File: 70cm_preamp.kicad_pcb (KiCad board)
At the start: 2 copper layers, 33 x 13.2 mm, 7 parts, among them J1 RF_IN, J2 RF_OUT, U1 SF2446E, U2 PGA-103+

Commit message: Stabilitáshoz RLC
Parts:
- added C1: 330p, 70cm_preamp:C_0603_1608Metric_Pad1.05x0.95mm_HandSolder, F.Cu at (63.1, 40.2)
- added L1: 620n, 70cm_preamp:L_0603_1608Metric_Pad1.05x0.95mm_HandSolder, F.Cu at (58.7, 37.7)
- added R1: 150, 70cm_preamp:R_0603_1608Metric_Pad1.05x0.95mm_HandSolder, F.Cu at (59.6, 40.2)
- moved U2 0.20 mm to (55.6, 38.3)
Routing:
- net Net-(C1-Pad1): track 0.00 -> 1.83 mm
- net Net-(L1-Pad2): track 0.00 -> 1.68 mm
- net GND: vias 28 -> 32

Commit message: 0805 RLC
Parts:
- C1: footprint 70cm_preamp:C_0603_1608Metric_Pad1.05x0.95mm_HandSolder -> 70cm_preamp:C_0805_2012Metric_Pad1.15x1.40mm_HandSolder
- L1: footprint 70cm_preamp:L_0603_1608Metric_Pad1.05x0.95mm_HandSolder -> 70cm_preamp:L_0805_2012Metric_Pad1.15x1.40mm_HandSolder
- R1: footprint 70cm_preamp:R_0603_1608Metric_Pad1.05x0.95mm_HandSolder -> 70cm_preamp:R_0805_2012Metric_Pad1.15x1.40mm_HandSolder
- moved U2 1.20 mm to (54.4, 38.3)
- moved R1 0.83 mm to (59.1, 40.9)
- moved C1 0.69 mm to (63.2, 40.9)
- moved L1 0.62 mm to (58.1, 37.8)
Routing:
- net Net-(L1-Pad1): track 3.38 -> 5.18 mm
- net Net-(J2-Pad1): track 6.50 -> 5.30 mm
- net GND: vias 32 -> 33

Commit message: Dokumentáció
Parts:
- moved C1 108.1 mm to (150.5, 104.7)
- moved J1 108.1 mm to (157.8, 100.7)
- moved J2 108.1 mm to (134.8, 100.7)
- moved R1 108.1 mm to (146.4, 104.7)
- moved G*** 108.1 mm to (134.8, 95.6)
- moved G*** 108.1 mm to (157.8, 95.6)
- moved G*** 108.1 mm to (146.3, 95.3)
- moved L1 108.1 mm to (145.3, 101.7)
- moved U1 108.1 mm to (149.6, 100.7)
- moved U2 108.1 mm to (141.6, 102.1)

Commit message: Add a few parts
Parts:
- removed G***: LOGO, 70cm_preamp:RCV
- removed G***: LOGO, 70cm_preamp:ANT
- removed G***: LOGO, 70cm_preamp:HA5KFU
- added C3: 330p, 70cm_preamp:C_0805_2012Metric_Pad1.15x1.40mm_HandSolder, F.Cu at (136.2, 105.4)
- added C4: 330p, 70cm_preamp:C_0805_2012Metric_Pad1.15x1.40mm_HandSolder, F.Cu at (134.2, 105.4)
- added C5: 330p, 70cm_preamp:C_0805_2012Metric_Pad1.15x1.40mm_HandSolder, F.Cu at (138.1, 105.4)
- added D2: LED, LED_SMD:LED_0805_2012Metric_Pad1.15x1.40mm_HandSolder, F.Cu at (131.0, 106.5)
- added L2: 620n, 70cm_preamp:L_0805_2012Metric_Pad1.15x1.40mm_HandSolder, F.Cu at (138.1, 101.6)
- added L3: 620n, 70cm_preamp:L_0805_2012Metric_Pad1.15x1.40mm_HandSolder, F.Cu at (131.1, 101.6)
- added R2: 330, 70cm_preamp:R_0805_2012Metric_Pad1.15x1.40mm_HandSolder, F.Cu at (126.0, 106.0)
- added U3: SF2446E, 70cm_preamp:SF2446E-Filter_Custom_HandSolder, F.Cu at (134.6, 100.6)
- moved J2 8.84 mm to (126.0, 100.7)
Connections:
- J2 pad 1: Net-(J2-Pad1) -> Net-(J2-In)
- U2 pad 3: Net-(J2-Pad1) -> Net-(JP1-A)
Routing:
- net Net-(D2-A): track 0.00 -> 12.5 mm
- net Net-(J2-In): track 0.00 -> 7.30 mm
- net Net-(J2-Pad1): track 5.30 -> 0.00 mm
- net Net-(JP1-A): track 0.00 -> 4.24 mm
- net Net-(D2-K): track 0.00 -> 3.16 mm
- net GND: vias 33 -> 52
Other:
- board size 33 x 13.2 mm -> 41.8 x 13.2 mm
- net class Default removed
- net class Tapvonal_vastag removed
- net class Tapvonal_vekony removed
- board text added: "HA5KFU HA8KDA 2023 MRC-100"
- board text added: "PWR"

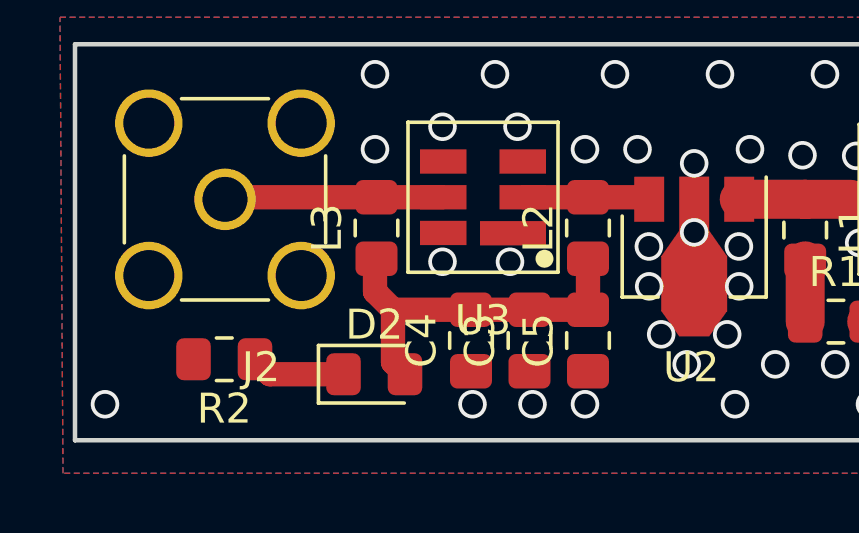
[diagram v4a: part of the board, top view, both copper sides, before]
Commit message: Improve inductor places and resolve throughPCB LED issues
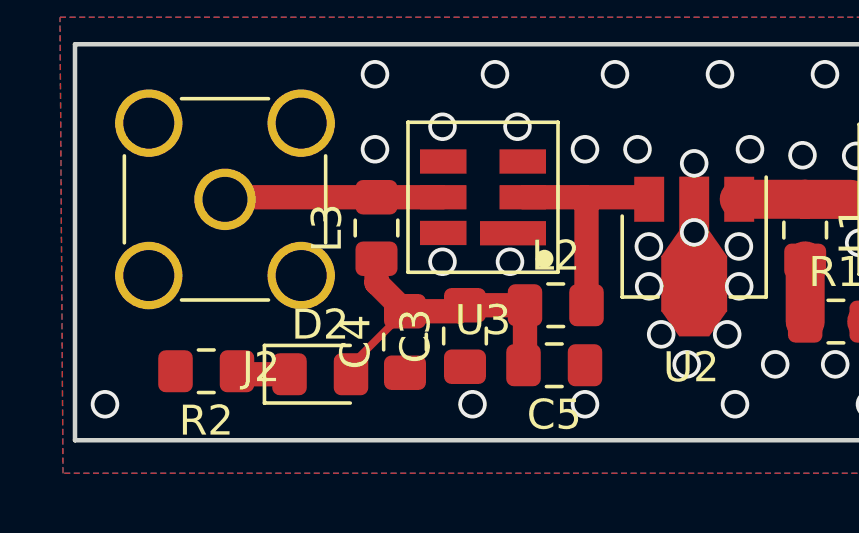
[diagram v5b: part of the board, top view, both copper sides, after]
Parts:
- moved L2 2.79 mm to (137.0, 104.2), turned to 0 degrees
- moved C4 2.20 mm to (132.0, 105.4)
- moved C3 2.16 mm to (134.0, 105.2)
- moved D2 1.80 mm to (129.2, 106.5)
- moved C5 1.40 mm to (137.0, 106.2), turned to 180 degrees
- moved R2 0.72 mm to (125.4, 106.4)
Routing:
- net Net-(JP1-A): track 4.24 -> 7.86 mm
- net Net-(D2-K): track 3.16 -> 1.79 mm
- net Net-(D2-A): track 12.5 -> 11.2 mm
- net GND: vias 52 -> 51

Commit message: final checks
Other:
- board text added: "ANT"
- board text added: "RCV"

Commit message: Label corrections
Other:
- board text added: "HA5KFU HA8KDA 2023 MRC-100 compatible"
- board text removed: "HA5KFU HA8KDA 2023 MRC-100"
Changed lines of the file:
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@@
     )
   )
-  (gr_line (start 131.572 102.108) (end 130.048 100.584)
+  (gr_line (start 134.112 105.156) (end 130.048 100.584)
     (stroke (width 0.8) (type default)) (layer "B.SilkS"))
-  (gr_line (start 136.652 102.108) (end 131.572 102.108)
+  (gr_line (start 139.192 105.156) (end 134.112 105.156)
     (stroke (width 0.8) (type default)) (layer "B.SilkS"))
   (gr_line (start 155.956 105.664) (end 157.988 103.632)
@@
   (gr_line (start 162.84 95.5) (end 162.84 108.7)
     (stroke (width 0.15) (type solid)) (layer "Edge.Cuts"))
-  (gr_text "HA5KFU HA8KDA 2023\n\nMRC-100" (at 151.5 101.5) (layer "B.SilkS")
+  (gr_text "HA5KFU HA8KDA 2023\n\nMRC-100 compatible" (at 151.5 101.5) (layer "B.SilkS")
     (effects (font (size 1 1) (thickness 0.15)) (justify left bottom mirror))
   )
@@
     (effects (font (size 1.5 1.5) (thickness 0.3) bold) (justify left bottom mirror))
   )
-  (gr_text "RCV" (at 136.652 101.6) (layer "B.SilkS")
+  (gr_text "RCV" (at 139.192 104.648) (layer "B.SilkS")
     (effects (font (size 1.5 1.5) (thickness 0.3) bold) (justify left bottom mirror))
   )
